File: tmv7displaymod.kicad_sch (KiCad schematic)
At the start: 10 parts, among them J1 DC IN +8 ... 15 V, J2 Conn_01x10, J3 Kenwood CAT Connector, U1 L7805, U4 ATmega8-16P

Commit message: Minor fixes and tweaks
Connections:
- no-connect marks 3 -> 18
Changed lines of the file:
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@@
   (junction (at 80.01 27.94) (diameter 0) (color 0 0 0 0)
   )
+  (no_connect (at 157.48 71.12))
   (no_connect (at 170.18 91.44))
-  (no_connect (at 102.87 44.45))
-  (no_connect (at 120.65 19.05))
+  (no_connect (at 157.48 63.5))
+  (no_connect (at 157.48 104.14))
+  (no_connect (at 157.48 106.68))
+  (no_connect (at 127 63.5))
+  (no_connect (at 157.48 99.06))
+  (no_connect (at 157.48 66.04))
+  (no_connect (at 127 73.66))
+  (no_connect (at 157.48 68.58))
+  (no_connect (at 127 68.58))
+  (no_connect (at 157.48 101.6))
+  (no_connect (at 157.48 111.76))
+  (no_connect (at 157.48 58.42))
+  (no_connect (at 157.48 109.22))
+  (no_connect (at 144.78 50.8))
+  (no_connect (at 144.78 121.92))
+  (no_connect (at 157.48 60.96))
   (wire (pts (xy 77.47 27.94) (xy 80.01 27.94))
     (stroke (width 0) (type default))

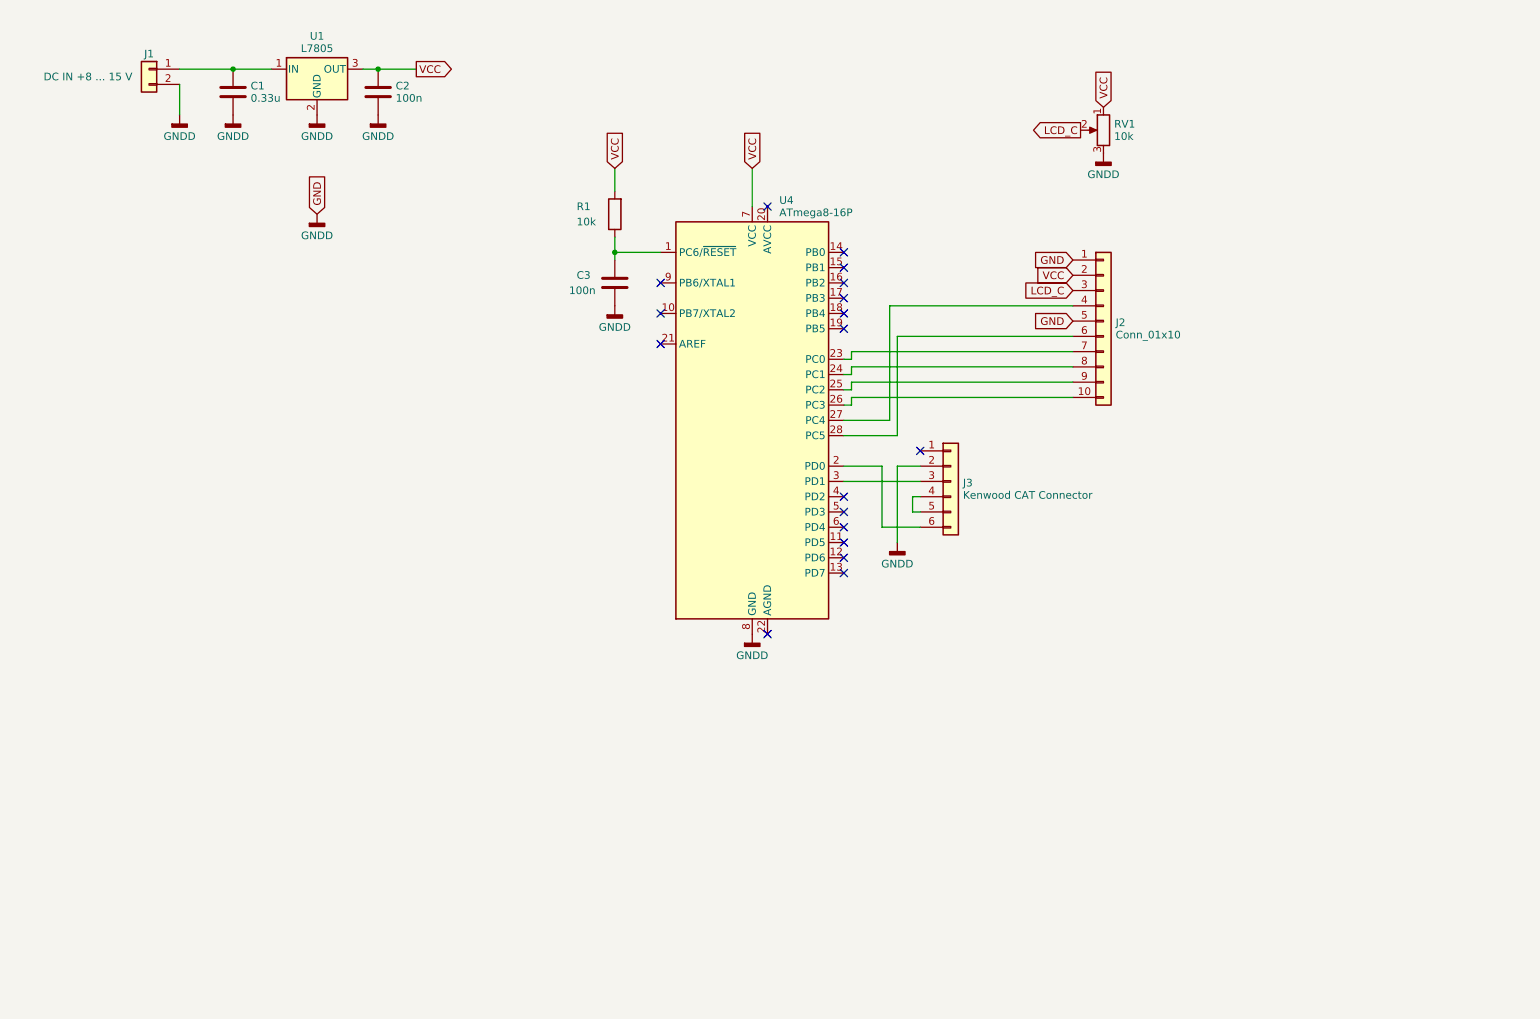
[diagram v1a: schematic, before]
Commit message: Additional tweaks. xchanged rs for e and added backlight.
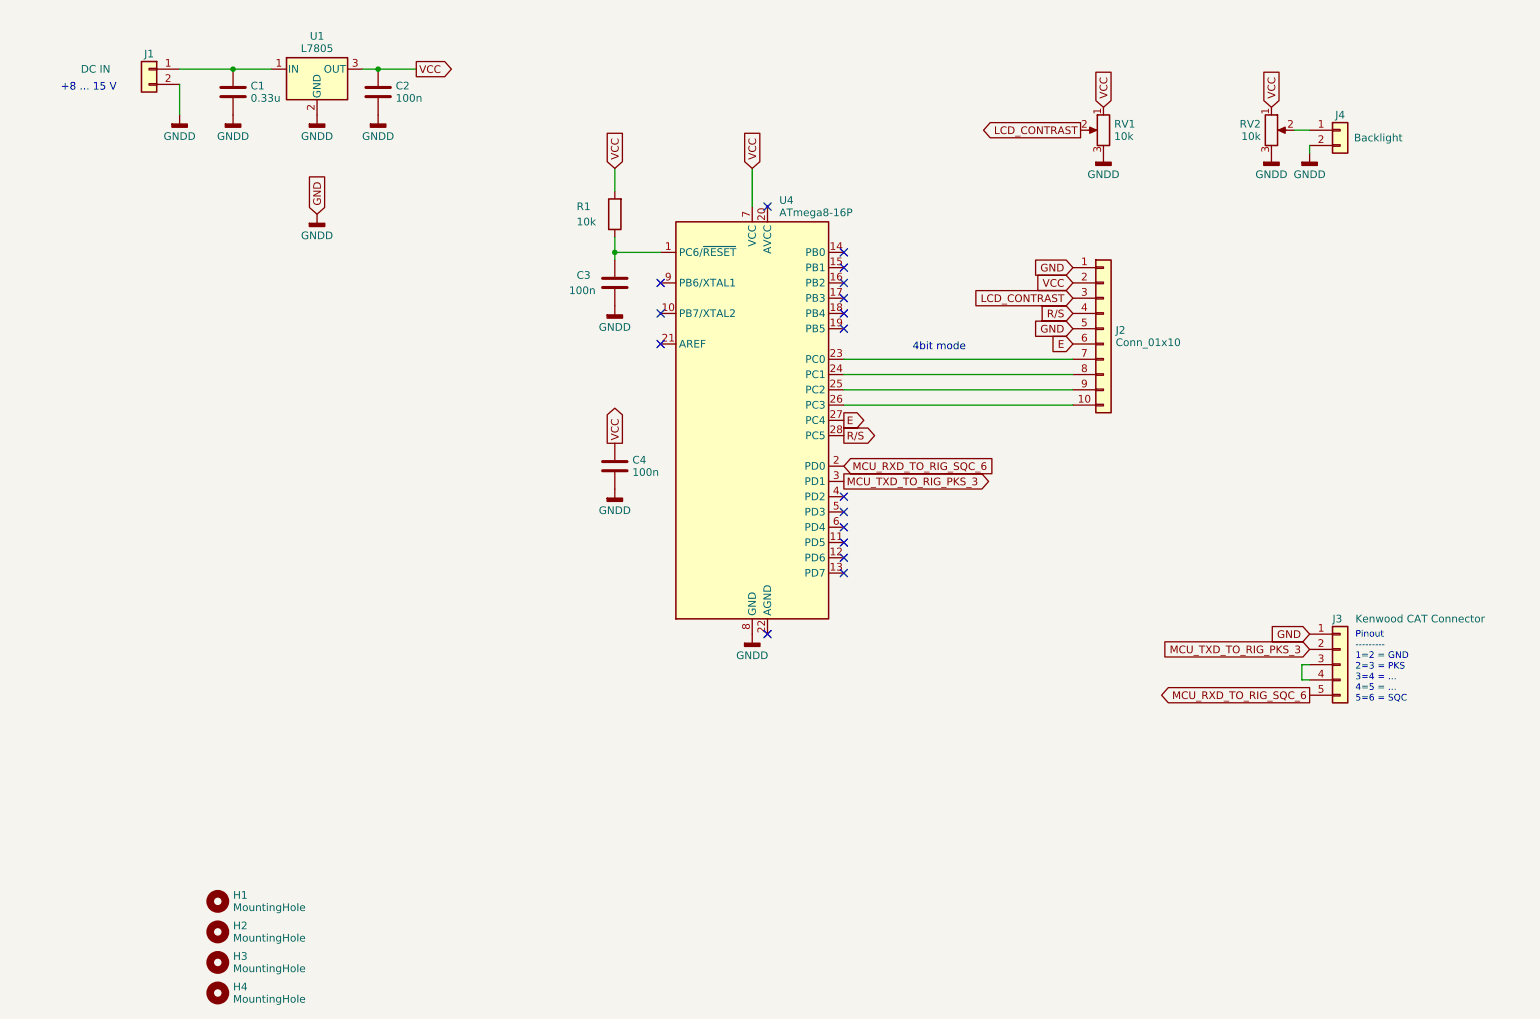
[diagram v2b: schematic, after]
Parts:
- added C4: 100n, Capacitor_THT:C_Disc_D3.8mm_W2.6mm_P2.50mm, symbol Device:C
- added H1, H2, H3, H4: MountingHole, MountingHole:MountingHole_2.2mm_M2_Pad_Via, symbol Mechanical:MountingHole
- added J4: Backlight, Connector_Molex:Molex_KK-254_AE-6410-02A_1x02_P2.54mm_Vertical, symbol Connector_Generic:Conn_01x02
- added RV2: 10k, Potentiometer_THT:Potentiometer_Bourns_3296W_Vertical, symbol Device:R_Potentiometer
- J1: value DC IN +8 ... 15 V -> DC IN
- J3: footprint Connector_Molex:Molex_KK-254_AE-6410-06A_1x06_P2.54mm_Vertical -> Connector_Molex:Molex_KK-254_AE-6410-05A_1x05_P2.54mm_Vertical; symbol Connector_Generic:Conn_01x06 -> Connector_Generic:Conn_01x05
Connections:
- net GNDD: now also J3.1 (Pin_1), C4.2, J4.2 (Pin_2), RV2.3; no longer J3.2 (Pin_2)
- net VCC: now also C4.1, RV2.1
- net at J3.3 (Pin_3): now also J3.4 (Pin_4); no longer U4.3 (PD1)
- net MCU_RXD_TO_RIG_SQC_6: now reaches J3.5 (Pin_5)
- net MCU_RXD_TO_RIG_SQC_6: now also U4.2 (PD0); no longer J3.4 (Pin_4)
- net E: now reaches U4.27 (PC4)
- net E: now also J2.6 (Pin_6); no longer J2.4 (Pin_4)
- net R/S: now reaches U4.28 (PC5)
- net R/S: now also J2.4 (Pin_4); no longer J2.6 (Pin_6)
- net LCD_C renamed LCD_CONTRAST
- new net: J4.1 (Pin_1), RV2.2
- new net MCU_TXD_TO_RIG_PKS_3: J3.2 (Pin_2), U4.3 (PD1)
- no-connect marks 18 -> 17
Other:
- note added: "+8 ... 15 V"
- note added: "4bit mode"
- note added: "Pinout --------- 1=2 = GND 2=3 = PKS 3=4 = ... 4=5 = ... 5=6 = SQC"
- moved on the sheet: J2

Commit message: V1.2 - minor tweaks and new exports. Organized exports
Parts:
- added SW1: RESET, Connector_PinHeader_2.54mm:PinHeader_1x02_P2.54mm_Vertical, symbol Switch:SW_Push
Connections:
- net GNDD: now also SW1.1
- net at C3.1, R1.1, U4.1 (PC6/~{RESET}): now also SW1.2
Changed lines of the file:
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@@
   (title_block
     (title "Kenwood TM-V7 Display Mod")
-    (date "2023-07-19")
-    (rev "0.1")
+    (date "2023-08-22")
+    (rev "1.2")
     (company "#pragma | CT1ENQ")
     (comment 1 "Schematic and PCB")
@@
   (no_connect (at 144.78 121.92))
   (no_connect (at 157.48 60.96))
+  (wire (pts (xy 102.87 58.42) (xy 102.87 67.31))
+    (stroke (width 0) (type default))
+  )
   (wire (pts (xy 234.95 40.64) (xy 234.95 41.91))
     (stroke (width 0) (type default))
@@
   )
   (wire (pts (xy 80.01 27.94) (xy 86.36 27.94))
+    (stroke (width 0) (type default))
+  )
+  (wire (pts (xy 113.03 58.42) (xy 119.38 58.42))
     (stroke (width 0) (type default))
   )
@@
         (path "/3ee868a6-cab0-4cb8-a7c3-1e1b42f068ba"
           (reference "C2") (unit 1)
+        )
+      )
+    )
+  )
+  (symbol (lib_id "Switch:SW_Push") (at 107.95 58.42 0) (unit 1)
+    (in_bom yes) (on_board yes) (dnp no) (fields_autoplaced)
+    (property "Reference" "SW1" (at 107.95 50.8 0)
+      (effects (font (size 1.27 1.27)))
+    )
+    (property "Value" "RESET" (at 107.95 53.34 0)
+      (effects (font (size 1.27 1.27)))
+    )
+    (property "Footprint" "Connector_PinHeader_2.54mm:PinHeader_1x02_P2.54mm_Vertical" (at 107.95 53.34 0)
+      (effects (font (size 1.27 1.27)) hide)
+    )
+    (property "Datasheet" "~" (at 107.95 53.34 0)
+      (effects (font (size 1.27 1.27)) hide)
+    )
+    (pin "1")
+    (pin "2")
+    (instances
+      (project "tmv7displaymod"
+        (path "/3ee868a6-cab0-4cb8-a7c3-1e1b42f068ba"
+          (reference "SW1") (unit 1)
         )
       )
@@
         )
       )
+    )
+  )
+  (symbol (lib_id "power:GNDD") (at 102.87 67.31 0) (unit 1)
+    (in_bom yes) (on_board yes) (dnp no) (fields_autoplaced)
+    (property "Reference" "#PWR012" (at 102.87 73.66 0)
+      (effects (font (size 1.27 1.27)) hide)
+    )
+    (property "Value" "GNDD" (at 102.87 70.874 0)
+      (effects (font (size 1.27 1.27)))
+    )
+    (property "Footprint" "" (at 102.87 67.31 0)
+      (effects (font (size 1.27 1.27)) hide)
+    )
+    (property "Datasheet" "" (at 102.87 67.31 0)
+      (effects (font (size 1.27 1.27)) hide)
+    )
+    (pin "1")
+    (instances
+      (project "tmv7displaymod"
+        (path "/3ee868a6-cab0-4cb8-a7c3-1e1b42f068ba"
+          (reference "#PWR012") (unit 1)
+        )
+      )

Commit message: More tweaks to v1.3
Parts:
- J1: value DC IN -> 2 Pin Molex/KK (DC In)
- J2: value Conn_01x10 -> 10 Pin Molex/KK (Display)
- J3: value Kenwood CAT Connector -> 5 Pin Molex/KK (Radio)
- J4: value Backlight -> 2 Pin Molex/kk (Backlight)
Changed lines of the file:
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@@
     (effects (font (size 1.1 1.1)) (justify left bottom))
   )
-  (text " +8 ... 15 V" (at 26.67 31.75 0)
+  (text " +8 ... 15 V" (at 26.67 30.48 0)
     (effects (font (size 1.27 1.27)) (justify left bottom))
   )
@@
       (effects (font (size 1.27 1.27)) (justify left))
     )
-    (property "Value" "Kenwood CAT Connector" (at 242.57 119.38 0)
+    (property "Value" "5 Pin Molex/KK (Radio)" (at 242.57 119.38 0)
       (effects (font (size 1.27 1.27)) (justify left))
     )
@@
       (effects (font (size 1.27 1.27)))
     )
-    (property "Value" "Backlight" (at 246.38 39.37 0)
+    (property "Value" "2 Pin Molex/kk (Backlight)" (at 255.27 39.37 0)
       (effects (font (size 1.27 1.27)))
     )
@@
       (effects (font (size 1.27 1.27)) (justify left))
     )
-    (property "Value" "Conn_01x10" (at 202.692 73.414 0)
+    (property "Value" "10 Pin Molex/KK (Display)" (at 202.692 73.414 0)
       (effects (font (size 1.27 1.27)) (justify left))
     )
@@
       (effects (font (size 1.27 1.27)))
     )
-    (property "Value" "DC IN" (at 33.02 27.94 0)
-      (effects (font (size 1.27 1.27)))
-    )
+    (property "Value" "2 Pin Molex/KK (DC In)" (at 33.02 34.29 0)
+      (effects (font (size 1.27 1.27)))
+    )
